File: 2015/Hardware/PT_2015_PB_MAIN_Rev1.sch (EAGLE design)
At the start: 11 parts, among them Q1 Q_INA28

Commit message: Uh, I forgot
I just saved it and now I’m committing the changes. I don’t exactly
remember what I did.
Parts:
- DOOKU-12V, VADER-5V: value Q_PTN78020 -> Q_PTN78020HAH
- renumbered U$1 to SIDEOUS-12V, U$2 to PALPATINE-12V, U$3 to VADER-5V, U$4 to DOOKU-12V
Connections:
- removed net N$3: C5.1, Q1.V+
- new net +5V: C5.1, Q1.REF2, Q1.V+
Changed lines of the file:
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@@
 </classes>
 <parts>
-<part name="U$1" library="MRDT-2015-PowerBoard" deviceset="UQW-12/20-T48NBS" device=""/>
-<part name="U$2" library="MRDT-2015-PowerBoard" deviceset="UQW-12/20-T48NBS" device=""/>
-<part name="U$3" library="MRDT-2015-PowerBoard" deviceset="Q_PTN78020" device=""/>
-<part name="U$4" library="MRDT-2015-PowerBoard" deviceset="Q_PTN78020" device=""/>
+<part name="SIDEOUS-12V" library="MRDT-2015-PowerBoard" deviceset="UQW-12/20-T48NBS" device=""/>
+<part name="PALPATINE-12V" library="MRDT-2015-PowerBoard" deviceset="UQW-12/20-T48NBS" device=""/>
+<part name="VADER-5V" library="MRDT-2015-PowerBoard" deviceset="Q_PTN78020" device="" value="Q_PTN78020HAH"/>
+<part name="DOOKU-12V" library="MRDT-2015-PowerBoard" deviceset="Q_PTN78020" device="" value="Q_PTN78020HAH"/>
 <part name="GND2" library="SparkFun-Aesthetics" deviceset="GND" device=""/>
 <part name="GND3" library="SparkFun-Aesthetics" deviceset="GND" device=""/>
@@
 <part name="GND1" library="SparkFun-Aesthetics" deviceset="GND" device=""/>
 <part name="C5" library="resistor" deviceset="C-US" device="C1206"/>
+<part name="P+1" library="supply1" deviceset="+5V" device=""/>
+<part name="P+2" library="supply1" deviceset="+5V" device=""/>
 </parts>
 <sheets>
@@
 </plain>
 <instances>
-<instance part="U$1" gate="G$1" x="63.5" y="73.66"/>
-<instance part="U$2" gate="G$1" x="63.5" y="43.18"/>
-<instance part="U$3" gate="G$1" x="45.72" y="12.7"/>
-<instance part="U$4" gate="G$1" x="45.72" y="119.38"/>
+<instance part="SIDEOUS-12V" gate="G$1" x="63.5" y="73.66"/>
+<instance part="PALPATINE-12V" gate="G$1" x="63.5" y="43.18"/>
+<instance part="VADER-5V" gate="G$1" x="45.72" y="12.7"/>
+<instance part="DOOKU-12V" gate="G$1" x="45.72" y="119.38"/>
 <instance part="GND2" gate="1" x="35.56" y="7.62"/>
 <instance part="GND3" gate="1" x="35.56" y="30.48"/>
@@
 <instance part="GND1" gate="1" x="-142.24" y="137.16"/>
 <instance part="C5" gate="G$1" x="-132.08" y="149.86"/>
+<instance part="P+1" gate="1" x="-139.7" y="177.8"/>
+<instance part="P+2" gate="1" x="-139.7" y="177.8"/>
 </instances>
 <busses>
@@
 <net name="GND" class="0">
 <segment>
-<pinref part="U$4" gate="G$1" pin="GND"/>
+<pinref part="DOOKU-12V" gate="G$1" pin="GND"/>
 <pinref part="GND5" gate="1" pin="GND"/>
 <wire x1="40.64" y1="119.38" x2="35.56" y2="119.38" width="0.1524" layer="91"/>
@@
 </segment>
 <segment>
-<pinref part="U$1" gate="G$1" pin="-VIN"/>
+<pinref part="SIDEOUS-12V" gate="G$1" pin="-VIN"/>
 <pinref part="GND4" gate="1" pin="GND"/>
 <wire x1="40.64" y1="66.04" x2="35.56" y2="66.04" width="0.1524" layer="91"/>
@@
 </segment>
 <segment>
-<pinref part="U$2" gate="G$1" pin="-VIN"/>
+<pinref part="PALPATINE-12V" gate="G$1" pin="-VIN"/>
 <wire x1="40.64" y1="35.56" x2="35.56" y2="35.56" width="0.1524" layer="91"/>
 <wire x1="35.56" y1="35.56" x2="35.56" y2="33.02" width="0.1524" layer="91"/>
@@
 </segment>
 <segment>
-<pinref part="U$3" gate="G$1" pin="GND"/>
+<pinref part="VADER-5V" gate="G$1" pin="GND"/>
 <pinref part="GND2" gate="1" pin="GND"/>
 <wire x1="40.64" y1="12.7" x2="35.56" y2="12.7" width="0.1524" layer="91"/>
@@
 <net name="V_BATT" class="0">
 <segment>
-<pinref part="U$3" gate="G$1" pin="VIN"/>
+<pinref part="VADER-5V" gate="G$1" pin="VIN"/>
 <pinref part="SUPPLY5" gate="G$1" pin="V_BATT"/>
 <wire x1="40.64" y1="0" x2="25.4" y2="0" width="0.1524" layer="91"/>
@@
 </segment>
 <segment>
-<pinref part="U$1" gate="G$1" pin="+VIN"/>
+<pinref part="SIDEOUS-12V" gate="G$1" pin="+VIN"/>
 <pinref part="SUPPLY3" gate="G$1" pin="V_BATT"/>
 <wire x1="40.64" y1="81.28" x2="25.4" y2="81.28" width="0.1524" layer="91"/>
@@
 </segment>
 <segment>
-<pinref part="U$2" gate="G$1" pin="+VIN"/>
+<pinref part="PALPATINE-12V" gate="G$1" pin="+VIN"/>
 <pinref part="SUPPLY4" gate="G$1" pin="V_BATT"/>
 <wire x1="40.64" y1="50.8" x2="25.4" y2="50.8" width="0.1524" layer="91"/>
@@
 </segment>
 <segment>
-<pinref part="U$4" gate="G$1" pin="VIN"/>
+<pinref part="DOOKU-12V" gate="G$1" pin="VIN"/>
 <pinref part="SUPPLY2" gate="G$1" pin="V_BATT"/>
 <wire x1="40.64" y1="106.68" x2="25.4" y2="106.68" width="0.1524" layer="91"/>
@@
 </segment>
 </net>
-<net name="N$3" class="0">
+<net name="+5V" class="0">
 <segment>
+<pinref part="P+1" gate="1" pin="+5V"/>
+<pinref part="P+2" gate="1" pin="+5V"/>
 <pinref part="Q1" gate="G$1" pin="V+"/>
 <pinref part="C5" gate="G$1" pin="1"/>
@@
 <wire x1="-139.7" y1="154.94" x2="-132.08" y2="154.94" width="0.1524" layer="91"/>
 <wire x1="-132.08" y1="154.94" x2="-132.08" y2="152.4" width="0.1524" layer="91"/>
-<wire x1="-139.7" y1="154.94" x2="-139.7" y2="165.1" width="0.1524" layer="91"/>
+<wire x1="-139.7" y1="154.94" x2="-139.7" y2="160.02" width="0.1524" layer="91"/>
+<pinref part="Q1" gate="G$1" pin="REF2"/>
+<wire x1="-144.78" y1="160.02" x2="-139.7" y2="160.02" width="0.1524" layer="91"/>
+<wire x1="-139.7" y1="160.02" x2="-139.7" y2="175.26" width="0.1524" layer="91"/>
 </segment>
 </net>

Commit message: Continued work
Added lots of stuff
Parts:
- added C10: .1uF, SparkFun-Retired:2.2UF-CERCAP-10009
- added C11, C12, C13, C15, C6: (no value), resistor:C-USC1206
- added L1, L2, L4, L5, L6, L7, L8: L_29F0429, MRDT-2014-All:L_29F0429
- added Q2: Q_INA28, MRDT-2014-All:Q_INA28
- added Q3: Q_LTC490, PCB0M1:Q_LTC490
- added Q4, Q5: Q_ACS711LC, MRDT-2015-PowerBoard:Q_ACS711LC
- added R2: (no value), MRDT-2014-All:R_FC4L110R001JER
- added R3: 70kΩ, resistor:R-US_R1206
- added R4: 10kΩ, resistor:R-US_R1206
- added R5, R6: 120 Ohm, SparkFun-Passives:RESISTOR1206
- added R7: (no value), resistor:R-US_R1206
- added R8: 21kΩ, resistor:R-US_R1206
- added U$1: 32U4_BREAKOUT, MRDT-2015-General:32U4_BREAKOUT
- added U$2, U$3: D_SD12T1G, MRDT-2014-All:D_SD12T1G
- added U$4: RJ45-8PTH, SparkFun-Connectors:RJ45-8PTH
- C1, C2, C3, C4: value C_POL12.5MM_NORMAL -> 1mF
- DOOKU-12V, VADER-5V: value Q_PTN78020HAH -> Q_PTN78020WAH
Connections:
- new net N$10: L1.5, L1.6, L1.7, L1.8
- new net N$11: L2.5, L2.6, L2.7, L2.8, R2.2
- new net N$12: Q2.+IN, R2.SENSE2
- new net N$13: Q2.-IN, R2.SENSE1
- new net N$14: Q3.Y, R6.2, U$4.1
- new net N$15: L4.1, L4.2, L4.3, L4.4, VADER-5V.SENSE, VADER-5V.VOUT
- new net N$16: C11.1, L4.5, L4.6, L4.7, L4.8, Q4.IP+, U$2.C
- new net N$17: Q2.OUT
- new net N$18: Q3.Z, R6.1, U$4.2
- new net N$19: Q3.B, R5.2, U$4.6
- new net N$20: Q3.A, R5.1, U$4.3
- new net N$21: Q3.D, U$1.D1/TX
- new net N$22: U$1.A1
- new net N$23: U$1.A2
- new net N$24: U$1.A3
- new net N$25: U$1.A4
- new net N$26: U$1.A5
- new net N$27: U$1.D4/A6
- new net N$28: U$1.D6~/A7
- new net N$29: U$1.D8/A8
- new net N$3: C13.2, L8.5, L8.6, L8.7, L8.8, VADER-5V.VIN
- new net N$30: U$1.D9~/A9
- new net N$31: U$1.D10~/A10
- new net N$32: U$1.D12/A11
- new net N$33: C12.1, Q4.IP-
- new net N$34: Q4.VIOUT
- new net N$35: R8.2, VADER-5V.ADJUST
- new net N$36: DOOKU-12V.SENSE, DOOKU-12V.VOUT, L1.1, L1.2, L1.3, L1.4, U$3.C
- new net N$4: PALPATINE-12V.REMOTE, SIDEOUS-12V.REMOTE
- new net N$5: L7.5, L7.6, L7.7, L7.8, PALPATINE-12V.+VIN
- new net N$6: L6.5, L6.6, L6.7, L6.8, SIDEOUS-12V.+VIN
- new net N$7: L2.1, L2.2, L2.3, L2.4, PALPATINE-12V.+VOUT, SIDEOUS-12V.+VOUT
- new net N$8: DOOKU-12V.VIN, L5.5, L5.6, L5.7, L5.8
- new net N$9: DOOKU-12V.ADJUST, R7.2
- new net RXD: Q3.R, U$1.D0/RX
- new net VIN-MEAS: R3.1, R4.2, U$1.A0
- net +5V: now also C10.1, C6.1, Q2.REF2, Q2.V+, Q3.VCC, Q4.VCC, U$1.VCC
- net GND: now also C11.2, C12.2, C13.1, C15.1, C6.2, DOOKU-12V.GND1, PALPATINE-12V.-VOUT, Q2.GND, Q2.REF1, Q3.GND, Q4.GND, R4.1, R8.1, SIDEOUS-12V.-VOUT, U$1.GND@1, U$1.GND@2, U$2.A, U$3.A, U$4.7, U$4.8, VADER-5V.GND1
- net V_BATT: now also C15.2, L5.1, L5.2, L5.3, L5.4, L6.1, L6.2, L6.3, L6.4, L7.1, L7.2, L7.3, L7.4, L8.1, L8.2, L8.3, L8.4, R3.2; no longer DOOKU-12V.VIN, PALPATINE-12V.+VIN, SIDEOUS-12V.+VIN, VADER-5V.VIN
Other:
- note added: "Power conditioning capacitance"
- note added: "Primary voltage monitoring"
- moved on the sheet: DOOKU-12V

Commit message: Finished up 12V Critical bus
Fully connected ‘dooku’ bus with ouput current sensor and input
filtering.
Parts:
- removed U$3: D_SD12T1G, MRDT-2014-All:D_SD12T1G
- added C14, C8, C9: (no value), resistor:C-USC1206
- added C7: 1uF, resistor:C-USC1206
- added U$5: D_SD12T1G, MRDT-2014-All:D_SD12T1G
- C10: value .1uF -> (none); device SparkFun-Retired:2.2UF-CERCAP-10009 -> resistor:C-USC1206
- renumbered DOOKU-12V to DOOKU-12V-CRIT, VADER-5V to VADER-5V-CRIT
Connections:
- new net N$37: C8.1, Q5.IP-
- new net N$39: Q5.VIOUT
- net +5V: now also C7.1, Q5.VCC; no longer C10.1
- net GND: now also C10.1, C14.1, C7.2, C8.2, C9.2, Q5.GND, R7.1, U$5.A; no longer U$3.A
- net N$10: now also C9.1, Q5.IP+, U$5.C
- net N$36: no longer U$3.C
- net N$8: now also C14.2
- net V_BATT: now also C10.2
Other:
- moved on the sheet: C10, L5, Q5

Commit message: Continued work
Added a MOSFet for the primary voltage busses and input terminals
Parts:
- added BATT-NEG, BATT-POS: TERMINAL_HOLE, MRDT-2015-PowerBoard:TERMINAL_HOLE
- added Q6: Q_IRFS7437PbF, MRDT-2015-PowerBoard:Q_IRF7437SMD
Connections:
- new net N$38: R2.1
- new net N$40: Q6.D, R1.1
- new net N$41: Q6.S
- new net N$42: Q6.G
- net GND: now also BATT-NEG.P$1
- net V_BATT: now also BATT-POS.P$1
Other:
- note added: "Power input"
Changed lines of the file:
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@@
 <layer number="54" name="bGND_GNDA" color="1" fill="9" visible="no" active="no"/>
 <layer number="56" name="wert" color="7" fill="1" visible="no" active="no"/>
+<layer number="57" name="tCAD" color="7" fill="1" visible="no" active="no"/>
 <layer number="90" name="Modules" color="5" fill="1" visible="yes" active="yes"/>
 <layer number="91" name="Nets" color="2" fill="1" visible="yes" active="yes"/>
@@
 <layer number="143" name="PMD" color="7" fill="1" visible="yes" active="yes"/>
 <layer number="144" name="Drill Legend" color="7" fill="1" visible="yes" active="yes"/>
+<layer number="150" name="Notes" color="7" fill="1" visible="yes" active="yes"/>
 <layer number="151" name="HeatSink" color="7" fill="1" visible="yes" active="yes"/>
 <layer number="152" name="_bDocu" color="7" fill="1" visible="yes" active="yes"/>
+<layer number="153" name="FabDoc1" color="7" fill="1" visible="yes" active="yes"/>
+<layer number="154" name="FabDoc2" color="7" fill="1" visible="yes" active="yes"/>
+<layer number="155" name="FabDoc3" color="7" fill="1" visible="yes" active="yes"/>
 <layer number="199" name="Contour" color="7" fill="1" visible="yes" active="yes"/>
 <layer number="200" name="200bmp" color="1" fill="10" visible="yes" active="yes"/>
@@
 <part name="C14" library="resistor" deviceset="C-US" device="C1206"/>
 <part name="GND9" library="SparkFun-Aesthetics" deviceset="GND" device=""/>
+<part name="BATT-POS" library="MRDT-2015-PowerBoard" deviceset="TERMINAL_HOLE" device=""/>
+<part name="BATT-NEG" library="MRDT-2015-PowerBoard" deviceset="TERMINAL_HOLE" device=""/>
+<part name="GND26" library="SparkFun-Aesthetics" deviceset="GND" device=""/>
+<part name="SUPPLY8" library="SparkFun-Aesthetics" deviceset="V_BATT" device=""/>
+<part name="Q6" library="MRDT-2015-PowerBoard" deviceset="Q_IRF*7437" device="SMD" value="Q_IRFS7437PbF"/>
 </parts>
 <sheets>
@@
 <wire x1="162.56" y1="193.04" x2="162.56" y2="172.72" width="0.1524" layer="97"/>
 <text x="88.9" y="205.74" size="1.778" layer="97">Power conditioning capacitance</text>
+<wire x1="-35.56" y1="172.72" x2="-35.56" y2="205.74" width="0.1524" layer="97"/>
+<wire x1="-35.56" y1="205.74" x2="20.32" y2="205.74" width="0.1524" layer="97"/>
+<wire x1="20.32" y1="205.74" x2="20.32" y2="172.72" width="0.1524" layer="97"/>
+<text x="-27.94" y="208.28" size="1.778" layer="97">Power input</text>
 </plain>
 <instances>
@@
 <instance part="C14" gate="G$1" x="35.56" y="129.54"/>
 <instance part="GND9" gate="1" x="66.04" y="93.98"/>
+<instance part="BATT-POS" gate="G$1" x="-15.24" y="182.88"/>
+<instance part="BATT-NEG" gate="G$1" x="5.08" y="182.88"/>
+<instance part="GND26" gate="1" x="5.08" y="175.26"/>
+<instance part="SUPPLY8" gate="G$1" x="-15.24" y="198.12"/>
+<instance part="Q6" gate="G$1" x="-195.58" y="127"/>
 </instances>
 <busses>
@@
 <pinref part="R7" gate="G$1" pin="1"/>
 <wire x1="66.04" y1="99.06" x2="66.04" y2="96.52" width="0.1524" layer="91"/>
+</segment>
+<segment>
+<pinref part="BATT-NEG" gate="G$1" pin="P$1"/>
+<pinref part="GND26" gate="1" pin="GND"/>
+<wire x1="5.08" y1="182.88" x2="5.08" y2="177.8" width="0.1524" layer="91"/>
 </segment>
 </net>
@@
 <pinref part="SUPPLY7" gate="G$1" pin="V_BATT"/>
 <wire x1="200.66" y1="187.96" x2="200.66" y2="185.42" width="0.1524" layer="91"/>
+</segment>
+<segment>
+<pinref part="BATT-POS" gate="G$1" pin="P$1"/>
+<wire x1="-15.24" y1="182.88" x2="-15.24" y2="177.8" width="0.1524" layer="91"/>
+<wire x1="-15.24" y1="177.8" x2="-25.4" y2="177.8" width="0.1524" layer="91"/>
+<wire x1="-25.4" y1="177.8" x2="-25.4" y2="195.58" width="0.1524" layer="91"/>
+<pinref part="SUPPLY8" gate="G$1" pin="V_BATT"/>
+<wire x1="-25.4" y1="195.58" x2="-15.24" y2="195.58" width="0.1524" layer="91"/>
+<wire x1="-15.24" y1="195.58" x2="-15.24" y2="198.12" width="0.1524" layer="91"/>
 </segment>
 </net>
@@
 </segment>
 </net>
+<net name="N$38" class="0">
+<segment>
+<pinref part="R2" gate="G$1" pin="1"/>
+<wire x1="157.48" y1="53.34" x2="170.18" y2="53.34" width="0.1524" layer="91"/>
+<wire x1="170.18" y1="53.34" x2="170.18" y2="48.26" width="0.1524" layer="91"/>
+<wire x1="170.18" y1="48.26" x2="205.74" y2="48.26" width="0.1524" layer="91"/>
+</segment>
+</net>
+<net name="N$40" class="0">
+<segment>
+<pinref part="R1" gate="G$1" pin="1"/>
+<pinref part="Q6" gate="G$1" pin="D"/>
+<wire x1="-193.04" y1="149.86" x2="-193.04" y2="134.62" width="0.1524" layer="91"/>
+</segment>
+</net>
+<net name="N$41" class="0">
+<segment>
+<pinref part="Q6" gate="G$1" pin="S"/>
+<wire x1="-193.04" y1="119.38" x2="-193.04" y2="101.6" width="0.1524" layer="91"/>
+</segment>
+</net>
+<net name="N$42" class="0">
+<segment>
+<pinref part="Q6" gate="G$1" pin="G"/>
+<wire x1="-203.2" y1="129.54" x2="-208.28" y2="129.54" width="0.1524" layer="91"/>
+<wire x1="-208.28" y1="129.54" x2="-208.28" y2="132.08" width="0.1524" layer="91"/>
+</segment>
+</net>

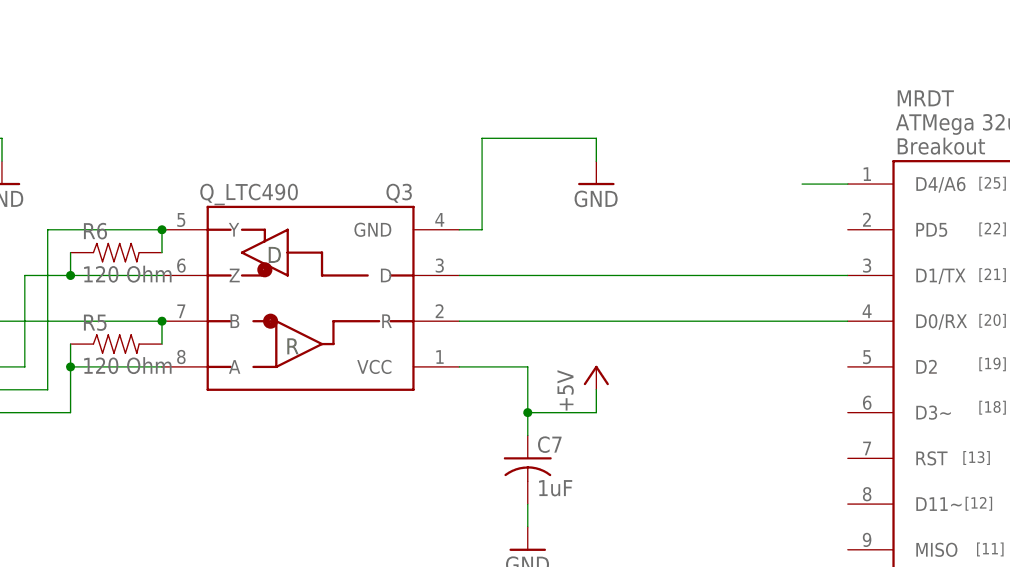
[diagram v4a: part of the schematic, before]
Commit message: Swapped the LTC490 with the Max3077
yes
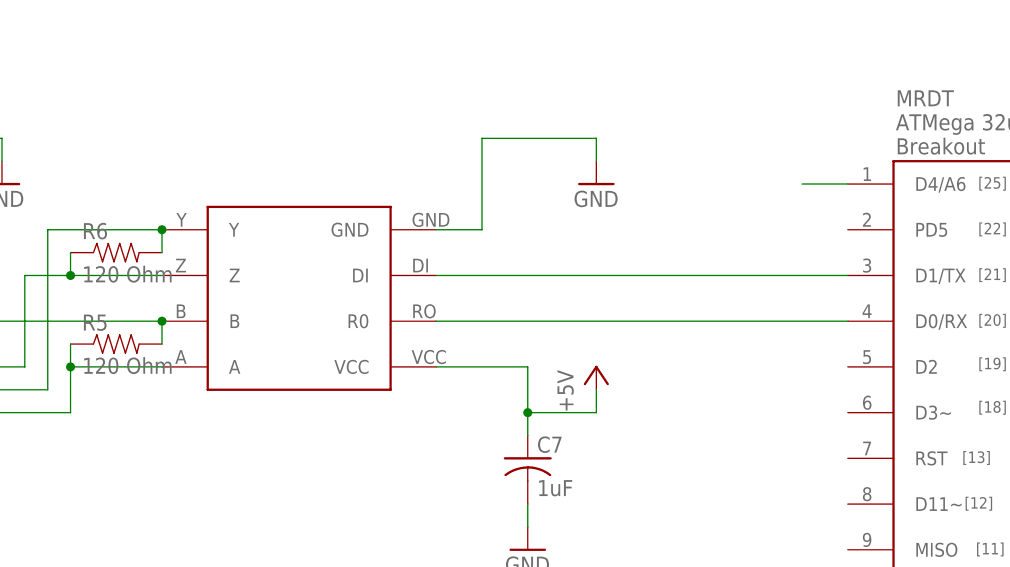
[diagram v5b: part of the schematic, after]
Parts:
- removed Q3: Q_LTC490, PCB0M1:Q_LTC490
- added U$3: MAX3077, MAX3077:MAX3077
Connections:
- net +5V: now also U$3.VCC; no longer Q3.VCC
- net GND: now also U$3.GND; no longer Q3.GND
- net N$14: now also U$3.Y; no longer Q3.Y
- net N$18: now also U$3.Z; no longer Q3.Z
- net N$19: now also U$3.B; no longer Q3.B
- net N$20: now also U$3.A; no longer Q3.A
- net N$21: now also U$3.DI; no longer Q3.D
- net RXD: now also U$3.R0; no longer Q3.R
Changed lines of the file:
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@@
 <part name="U$4" library="SparkFun-Connectors" deviceset="RJ45-8" device="PTH"/>
 <part name="R5" library="SparkFun-Passives" deviceset="RESISTOR" device="1206" value="120 Ohm"/>
-<part name="Q3" library="PCB0M1" deviceset="Q_LTC490" device=""/>
 <part name="R6" library="SparkFun-Passives" deviceset="RESISTOR" device="1206" value="120 Ohm"/>
 <part name="GND16" library="SparkFun-Aesthetics" deviceset="GND" device=""/>
@@
 <part name="SUPPLY8" library="SparkFun-Aesthetics" deviceset="V_BATT" device=""/>
 <part name="Q6" library="MRDT-2015-PowerBoard" deviceset="Q_IRF*7437" device="SMD" value="Q_IRFS7437PbF"/>
+<part name="U$3" library="MAX3077" deviceset="MAX3077" device=""/>
 </parts>
 <sheets>
@@
 <instance part="U$4" gate="G$1" x="-330.2" y="-60.96" rot="R180"/>
 <instance part="R5" gate="G$1" x="-297.18" y="-66.04"/>
-<instance part="Q3" gate="G$1" x="-266.7" y="-58.42" rot="R180"/>
 <instance part="R6" gate="G$1" x="-297.18" y="-55.88"/>
 <instance part="GND16" gate="1" x="-243.84" y="-48.26"/>
@@
 <instance part="SUPPLY8" gate="G$1" x="-15.24" y="198.12"/>
 <instance part="Q6" gate="G$1" x="-195.58" y="127"/>
+<instance part="U$3" gate="G$1" x="-276.86" y="-60.96" rot="R180"/>
 </instances>
 <busses>
@@
 <wire x1="-243.84" y1="-43.18" x2="-243.84" y2="-45.72" width="0.1524" layer="91"/>
 <pinref part="GND16" gate="1" pin="GND"/>
-<pinref part="Q3" gate="G$1" pin="GND"/>
-<wire x1="-256.54" y1="-53.34" x2="-259.08" y2="-53.34" width="0.1524" layer="91"/>
+<wire x1="-256.54" y1="-53.34" x2="-261.62" y2="-53.34" width="0.1524" layer="91"/>
+<pinref part="U$3" gate="G$1" pin="GND"/>
 </segment>
 <segment>
@@
 </segment>
 <segment>
-<pinref part="Q3" gate="G$1" pin="VCC"/>
-<wire x1="-259.08" y1="-68.58" x2="-251.46" y2="-68.58" width="0.1524" layer="91"/>
+<wire x1="-261.62" y1="-68.58" x2="-251.46" y2="-68.58" width="0.1524" layer="91"/>
 <wire x1="-251.46" y1="-68.58" x2="-251.46" y2="-73.66" width="0.1524" layer="91"/>
 <pinref part="P+6" gate="1" pin="+5V"/>
@@
 <junction x="-251.46" y="-73.66"/>
 <pinref part="C7" gate="G$1" pin="1"/>
+<pinref part="U$3" gate="G$1" pin="VCC"/>
 </segment>
 <segment>
@@
 <segment>
 <pinref part="U$1" gate="G$1" pin="D0/RX"/>
-<wire x1="-215.9" y1="-63.5" x2="-259.08" y2="-63.5" width="0.1524" layer="91"/>
-<pinref part="Q3" gate="G$1" pin="R"/>
+<wire x1="-215.9" y1="-63.5" x2="-261.62" y2="-63.5" width="0.1524" layer="91"/>
+<pinref part="U$3" gate="G$1" pin="R0"/>
 </segment>
 </net>
 <net name="N$14" class="0">
 <segment>
-<pinref part="Q3" gate="G$1" pin="Y"/>
 <wire x1="-292.1" y1="-53.34" x2="-304.8" y2="-53.34" width="0.1524" layer="91"/>
 <wire x1="-304.8" y1="-53.34" x2="-304.8" y2="-71.12" width="0.1524" layer="91"/>
@@
 <pinref part="R6" gate="G$1" pin="2"/>
 <wire x1="-292.1" y1="-53.34" x2="-292.1" y2="-55.88" width="0.1524" layer="91"/>
+<pinref part="U$3" gate="G$1" pin="Y"/>
 <junction x="-292.1" y="-53.34"/>
 </segment>
@@
 <net name="N$18" class="0">
 <segment>
-<pinref part="Q3" gate="G$1" pin="Z"/>
 <wire x1="-292.1" y1="-58.42" x2="-302.26" y2="-58.42" width="0.1524" layer="91"/>
 <wire x1="-302.26" y1="-58.42" x2="-307.34" y2="-58.42" width="0.1524" layer="91"/>
@@
 <wire x1="-302.26" y1="-55.88" x2="-302.26" y2="-58.42" width="0.1524" layer="91"/>
 <junction x="-302.26" y="-58.42"/>
+<pinref part="U$3" gate="G$1" pin="Z"/>
 </segment>
 </net>
 <net name="N$19" class="0">
 <segment>
-<pinref part="Q3" gate="G$1" pin="B"/>
 <wire x1="-292.1" y1="-63.5" x2="-312.42" y2="-63.5" width="0.1524" layer="91"/>
 <wire x1="-312.42" y1="-63.5" x2="-312.42" y2="-58.42" width="0.1524" layer="91"/>
@@
 <pinref part="R5" gate="G$1" pin="2"/>
 <wire x1="-292.1" y1="-63.5" x2="-292.1" y2="-66.04" width="0.1524" layer="91"/>
+<pinref part="U$3" gate="G$1" pin="B"/>
 <junction x="-292.1" y="-63.5"/>
 </segment>
@@
 <net name="N$20" class="0">
 <segment>
-<pinref part="Q3" gate="G$1" pin="A"/>
 <wire x1="-292.1" y1="-68.58" x2="-302.26" y2="-68.58" width="0.1524" layer="91"/>
 <wire x1="-302.26" y1="-68.58" x2="-302.26" y2="-73.66" width="0.1524" layer="91"/>
@@
 <wire x1="-302.26" y1="-66.04" x2="-302.26" y2="-68.58" width="0.1524" layer="91"/>
 <junction x="-302.26" y="-68.58"/>
+<pinref part="U$3" gate="G$1" pin="A"/>
 </segment>
 </net>
 <net name="N$21" class="0">
 <segment>
-<pinref part="Q3" gate="G$1" pin="D"/>
 <pinref part="U$1" gate="G$1" pin="D1/TX"/>
-<wire x1="-259.08" y1="-58.42" x2="-215.9" y2="-58.42" width="0.1524" layer="91"/>
-</segment>
-</net>
+<wire x1="-261.62" y1="-58.42" x2="-215.9" y2="-58.42" width="0.1524" layer="91"/>
+<pinref part="U$3" gate="G$1" pin="DI"/>
+</segment>
+</net>
